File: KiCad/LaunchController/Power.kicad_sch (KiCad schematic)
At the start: 39 parts, among them J1 DC_IN, J1 FROM_CONVERTER, J1 TO_CONVERTER, Q1 TJ8S06M3L, Q2 2SC3325-Y, Q3 TJ8S06M3L, U3 INA219BIDCNT, U5 INA219BIDCNT

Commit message: ロードスイッチの抵抗値を調整
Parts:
- R6: value 2.2kR -> 22kR
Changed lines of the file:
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@@
       (effects (font (size 1.27 1.27)))
     )
-    (property "Value" "2.2kR" (at 105.41 52.07 90)
+    (property "Value" "22kR" (at 105.41 52.07 90)
       (effects (font (size 1.27 1.27)))
     )

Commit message: ロードスイッチ駆動用のトランジスタのベース抵抗を10kRに修正
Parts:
- R6: value 22kR -> 10kR
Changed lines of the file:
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@@
       (effects (font (size 1.27 1.27)))
     )
-    (property "Value" "22kR" (at 105.41 52.07 90)
+    (property "Value" "10kR" (at 105.41 52.07 90)
       (effects (font (size 1.27 1.27)))
     )

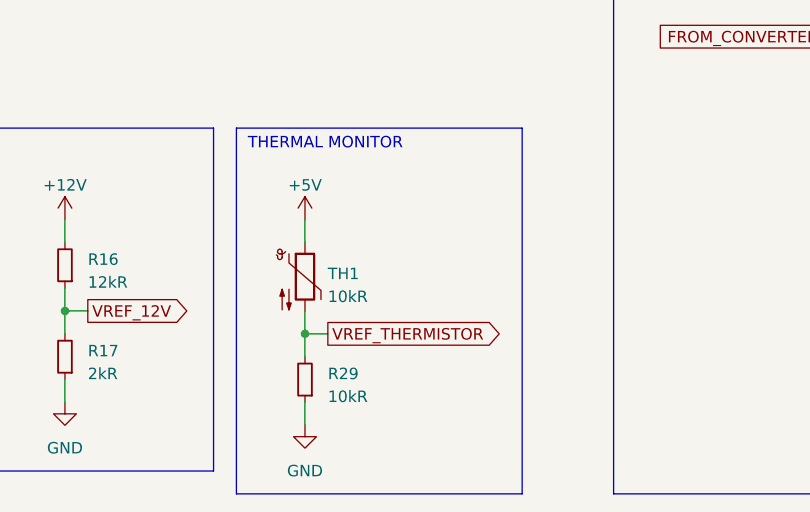
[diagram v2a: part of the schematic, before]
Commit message: サーミスタを分圧の下流側に変更
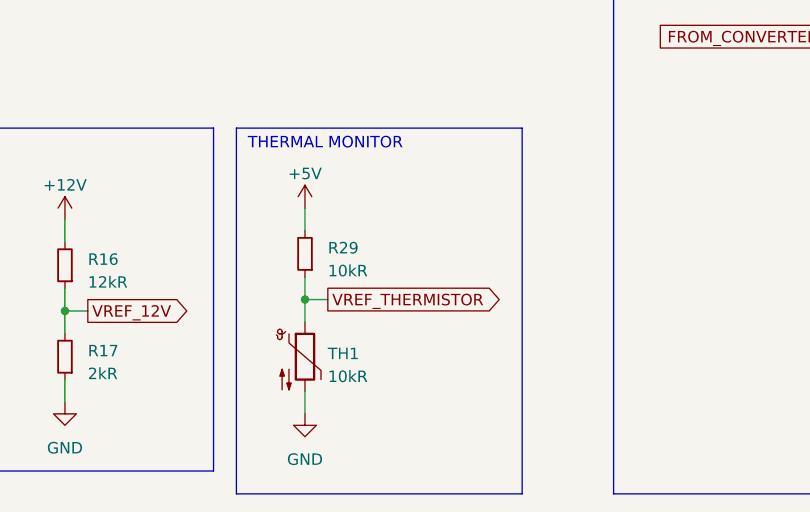
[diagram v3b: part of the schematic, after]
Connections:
- net +5V: now also R29.2; no longer TH1.1
- net GND: now also TH1.2; no longer R29.1
- net VREF_THERMISTOR: now also R29.1, TH1.1; no longer R29.2, TH1.2
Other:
- moved on the sheet: R29, TH1
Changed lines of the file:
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@@
   (junction (at 34.29 105.41) (diameter 0) (color 0 0 0 0)
   )
-  (junction (at 166.37 123.19) (diameter 0) (color 0 0 0 0)
-  )
   (junction (at 250.19 100.33) (diameter 0) (color 0 0 0 0)
   )
@@
   (junction (at 115.57 120.65) (diameter 0) (color 0 0 0 0)
   )
+  (junction (at 166.37 119.38) (diameter 0) (color 0 0 0 0)
+  )
   (junction (at 69.85 26.67) (diameter 0) (color 0 0 0 0)
   )
@@
     (stroke (width 0) (type default))
   )
+  (wire (pts (xy 166.37 119.38) (xy 166.37 121.92))
+    (stroke (width 0) (type default))
+  )
   (wire (pts (xy 100.33 54.61) (xy 97.79 54.61))
     (stroke (width 0) (type default))
@@
     (stroke (width 0) (type default))
   )
-  (wire (pts (xy 166.37 110.49) (xy 166.37 113.03))
-    (stroke (width 0) (type default))
-  )
   (wire (pts (xy 139.7 34.29) (xy 139.7 36.83))
     (stroke (width 0) (type default))
   )
-  (wire (pts (xy 166.37 123.19) (xy 166.37 125.73))
-    (stroke (width 0) (type default))
-  )
   (wire (pts (xy 38.1 62.23) (xy 40.64 62.23))
     (stroke (width 0) (type default))
@@
     (stroke (width 0) (type default))
   )
+  (wire (pts (xy 166.37 116.84) (xy 166.37 119.38))
+    (stroke (width 0) (type default))
+  )
   (wire (pts (xy 34.29 93.98) (xy 31.75 93.98))
     (stroke (width 0) (type default))
@@
     (stroke (width 0) (type default))
   )
-  (wire (pts (xy 166.37 123.19) (xy 168.91 123.19))
+  (wire (pts (xy 166.37 119.38) (xy 168.91 119.38))
     (stroke (width 0) (type default))
   )
@@
     (stroke (width 0) (type default))
   )
+  (wire (pts (xy 166.37 109.22) (xy 166.37 111.76))
+    (stroke (width 0) (type default))
+  )
   (wire (pts (xy 102.87 36.83) (xy 90.17 36.83))
     (stroke (width 0) (type default))
@@
     (stroke (width 0) (type default))
   )
-  (wire (pts (xy 166.37 130.81) (xy 166.37 133.35))
-    (stroke (width 0) (type default))
-  )
   (wire (pts (xy 165.1 41.91) (xy 165.1 44.45))
     (stroke (width 0) (type default))
@@
     (stroke (width 0) (type default))
   )
+  (wire (pts (xy 166.37 132.08) (xy 166.37 129.54))
+    (stroke (width 0) (type default))
+  )
   (wire (pts (xy 257.81 35.56) (xy 255.27 35.56))
     (stroke (width 0) (type default))
@@
   )
   (wire (pts (xy 165.1 34.29) (xy 175.26 34.29))
-    (stroke (width 0) (type default))
-  )
-  (wire (pts (xy 166.37 120.65) (xy 166.37 123.19))
     (stroke (width 0) (type default))
   )
@@
     )
   )
-  (global_label "VREF_THERMISTOR" (shape output) (at 168.91 123.19 0) (fields_autoplaced)
+  (global_label "VREF_THERMISTOR" (shape output) (at 168.91 119.38 0) (fields_autoplaced)
     (effects (font (size 1.27 1.27)) (justify left))
-    (property "Intersheetrefs" "${INTERSHEET_REFS}" (at 188.9305 123.19 0)
+    (property "Intersheetrefs" "${INTERSHEET_REFS}" (at 188.9305 119.38 0)
       (effects (font (size 1.27 1.27)) (justify left) hide)
     )
@@
     )
   )
-  (symbol (lib_id "Device:R_Small") (at 166.37 128.27 180) (unit 1)
-    (in_bom yes) (on_board yes) (dnp no) (fields_autoplaced)
-    (property "Reference" "R29" (at 168.91 127.635 0)
-      (effects (font (size 1.27 1.27)) (justify right))
-    )
-    (property "Value" "10kR" (at 168.91 130.175 0)
-      (effects (font (size 1.27 1.27)) (justify right))
-    )
-    (property "Footprint" "Resistor_SMD:R_0603_1608Metric_Pad0.98x0.95mm_HandSolder" (at 166.37 128.27 0)
-      (effects (font (size 1.27 1.27)) hide)
-    )
-    (property "Datasheet" "https://www.chip1stop.com/view/dispDetail/DispDetail?partId=ROHM-0021098" (at 166.37 128.27 0)
-      (effects (font (size 1.27 1.27)) hide)
-    )
-    (property "LCSC" "" (at 166.37 128.27 0)
+  (symbol (lib_id "Device:R_Small") (at 166.37 114.3 180) (unit 1)
+    (in_bom yes) (on_board yes) (dnp no) (fields_autoplaced)
+    (property "Reference" "R29" (at 168.91 113.665 0)
+      (effects (font (size 1.27 1.27)) (justify right))
+    )
+    (property "Value" "10kR" (at 168.91 116.205 0)
+      (effects (font (size 1.27 1.27)) (justify right))
+    )
+    (property "Footprint" "Resistor_SMD:R_0603_1608Metric_Pad0.98x0.95mm_HandSolder" (at 166.37 114.3 0)
+      (effects (font (size 1.27 1.27)) hide)
+    )
+    (property "Datasheet" "https://www.chip1stop.com/view/dispDetail/DispDetail?partId=ROHM-0021098" (at 166.37 114.3 0)
+      (effects (font (size 1.27 1.27)) hide)
+    )
+    (property "LCSC" "" (at 166.37 114.3 0)
       (effects (font (size 1.27 1.27)) hide)
     )
@@
     )
   )
-  (symbol (lib_id "Device:Thermistor_NTC") (at 166.37 116.84 0) (unit 1)
-    (in_bom yes) (on_board yes) (dnp no) (fields_autoplaced)
-    (property "Reference" "TH1" (at 168.91 116.5225 0)
-      (effects (font (size 1.27 1.27)) (justify left))
-    )
-    (property "Value" "10kR" (at 168.91 119.0625 0)
-      (effects (font (size 1.27 1.27)) (justify left))
-    )
-    (property "Footprint" "Resistor_SMD:R_0603_1608Metric_Pad0.98x0.95mm_HandSolder" (at 166.37 115.57 0)
-      (effects (font (size 1.27 1.27)) hide)
-    )
-    (property "Datasheet" "https://akizukidenshi.com/catalog/g/gP-05252/" (at 166.37 115.57 0)
-      (effects (font (size 1.27 1.27)) hide)
-    )
-    (property "LCSC" "" (at 166.37 116.84 0)
+  (symbol (lib_id "Device:Thermistor_NTC") (at 166.37 125.73 0) (unit 1)
+    (in_bom yes) (on_board yes) (dnp no) (fields_autoplaced)
+    (property "Reference" "TH1" (at 168.91 125.4125 0)
+      (effects (font (size 1.27 1.27)) (justify left))
+    )
+    (property "Value" "10kR" (at 168.91 127.9525 0)
+      (effects (font (size 1.27 1.27)) (justify left))
+    )
+    (property "Footprint" "Resistor_SMD:R_0603_1608Metric_Pad0.98x0.95mm_HandSolder" (at 166.37 124.46 0)
+      (effects (font (size 1.27 1.27)) hide)
+    )
+    (property "Datasheet" "https://akizukidenshi.com/catalog/g/gP-05252/" (at 166.37 124.46 0)
+      (effects (font (size 1.27 1.27)) hide)
+    )
+    (property "LCSC" "" (at 166.37 125.73 0)
       (effects (font (size 1.27 1.27)) hide)
     )
@@
     )
   )
-  (symbol (lib_id "power:+5V") (at 166.37 110.49 0) (unit 1)
-    (in_bom yes) (on_board yes) (dnp no) (fields_autoplaced)
-    (property "Reference" "#PWR052" (at 166.37 114.3 0)
-      (effects (font (size 1.27 1.27)) hide)
-    )
-    (property "Value" "+5V" (at 166.37 106.68 0)
+  (symbol (lib_id "power:+5V") (at 166.37 109.22 0) (unit 1)
+    (in_bom yes) (on_board yes) (dnp no) (fields_autoplaced)
+    (property "Reference" "#PWR052" (at 166.37 113.03 0)
+      (effects (font (size 1.27 1.27)) hide)
+    )
+    (property "Value" "+5V" (at 166.37 105.41 0)
       (effects (font (size 1.27 1.27)))
     )
-    (property "Footprint" "" (at 166.37 110.49 0)
-      (effects (font (size 1.27 1.27)) hide)
-    )
-    (property "Datasheet" "" (at 166.37 110.49 0)
+    (property "Footprint" "" (at 166.37 109.22 0)
+      (effects (font (size 1.27 1.27)) hide)
+    )
+    (property "Datasheet" "" (at 166.37 109.22 0)
       (effects (font (size 1.27 1.27)) hide)
     )
@@
     )
   )
-  (symbol (lib_id "power:GND") (at 166.37 133.35 0) (unit 1)
-    (in_bom yes) (on_board yes) (dnp no) (fields_autoplaced)
-    (property "Reference" "#PWR?" (at 166.37 139.7 0)
-      (effects (font (size 1.27 1.27)) hide)
-    )
-    (property "Value" "GND" (at 166.37 138.43 0)
+  (symbol (lib_id "power:GND") (at 166.37 132.08 0) (unit 1)
+    (in_bom yes) (on_board yes) (dnp no) (fields_autoplaced)
+    (property "Reference" "#PWR?" (at 166.37 138.43 0)
+      (effects (font (size 1.27 1.27)) hide)
+    )
+    (property "Value" "GND" (at 166.37 137.16 0)
       (effects (font (size 1.27 1.27)))
     )
-    (property "Footprint" "" (at 166.37 133.35 0)
-      (effects (font (size 1.27 1.27)) hide)
-    )
-    (property "Datasheet" "" (at 166.37 133.35 0)
-      (effects (font (size 1.27 1.27)) hide)
-    )
+    (property "Footprint" "" (at 166.37 132.08 0)
+      (effects (font (size 1.27 1.27)) hide)
+    )
+    (property "Datasheet" "" (at 166.37 132.08 0)
+      (effects (font (size 1.27 1.27)) hide)
+    )

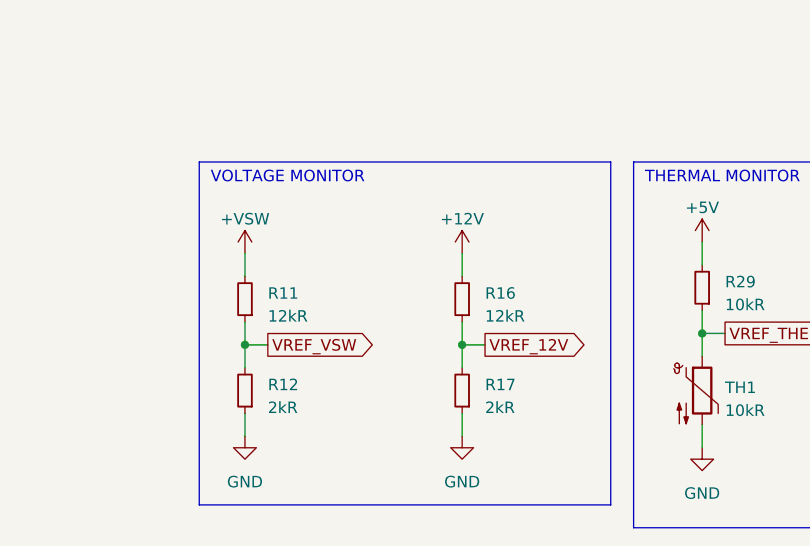
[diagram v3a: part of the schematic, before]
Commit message: イラン分圧回路を削除
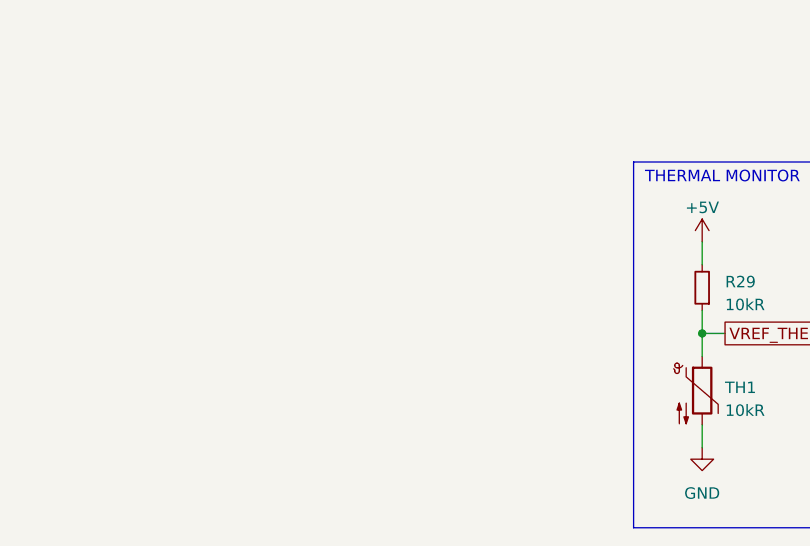
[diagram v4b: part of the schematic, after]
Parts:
- removed R11, R16: 12kR, Resistor_SMD:R_0603_1608Metric_Pad0.98x0.95mm_HandSolder, symbol Device:R_Small
- removed R12, R17: 2kR, Resistor_SMD:R_0603_1608Metric_Pad0.98x0.95mm_HandSolder, symbol Device:R_Small
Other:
- note removed: "VOLTAGE MONITOR"

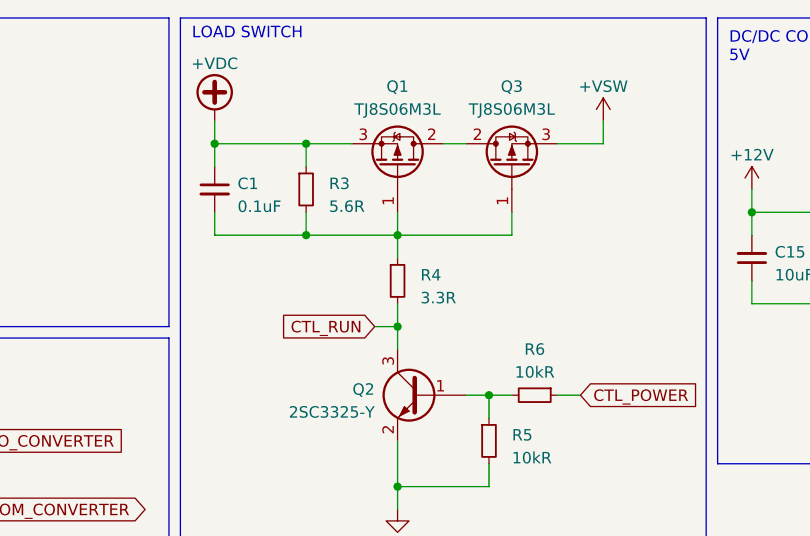
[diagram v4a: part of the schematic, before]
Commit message: 抵抗値を修正
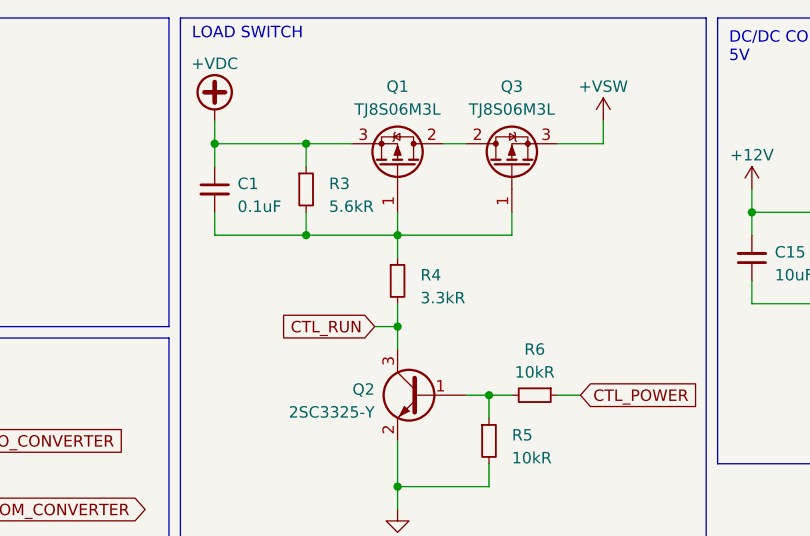
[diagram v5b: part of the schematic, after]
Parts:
- R3: value 5.6R -> 5.6kR
- R4: value 3.3R -> 3.3kR
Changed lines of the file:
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@@
       (effects (font (size 1.27 1.27)) (justify left))
     )
-    (property "Value" "5.6R" (at 82.55 33.655 0)
+    (property "Value" "5.6kR" (at 82.55 33.655 0)
       (effects (font (size 1.27 1.27)) (justify left))
     )
@@
       (effects (font (size 1.27 1.27)) (justify left))
     )
-    (property "Value" "3.3R" (at 92.71 43.815 0)
-      (effects (font (size 1.27 1.27)) (justify left))
-    )
+    (property "Value" "3.3kR" (at 92.71 43.815 0)
+      (effects (font (size 1.27 1.27)) (justify left))
+    )

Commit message: KiCad9.0に対応
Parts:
- gave numbers to parts that had none: 1
- renumbered C1 to C12, C5 to C13, C15 to C14, C16 to C15, C17 to C16, C18 to C17, C14 to C18, D6 to D5, D5 to D6, J1 to J4, J1 to J5, J1 to J6, Q3 to Q2, Q2 to Q3, R3 to R11, R4 to R12, R7 to R13, R6 to R14, R9 to R15, R10 to R16, R5 to R17, R21 to R18, R23 to R21, R24 to R22, R29 to R25, TP8 to TP2, TP15 to TP3, TP2 to TP4, U3 to U4
